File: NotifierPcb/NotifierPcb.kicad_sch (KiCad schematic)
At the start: 29 parts, among them IC1 CD4067BEE4, IC2 ESP32-WROOM-32E__8MB_, J1 RC_433_MHZ_RF, J2 UART_Conn, J3 Power_Conn, U1 HT75xx-1-SOT89

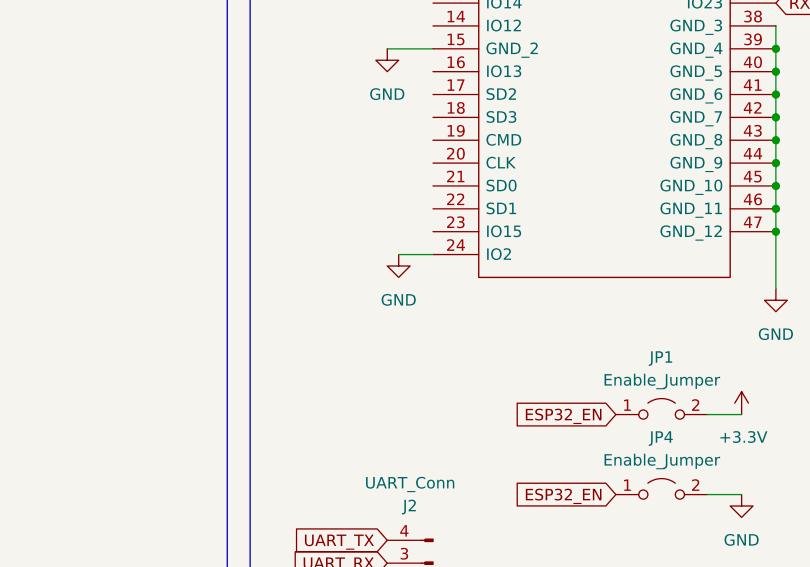
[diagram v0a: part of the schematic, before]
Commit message: reroute GND for headers
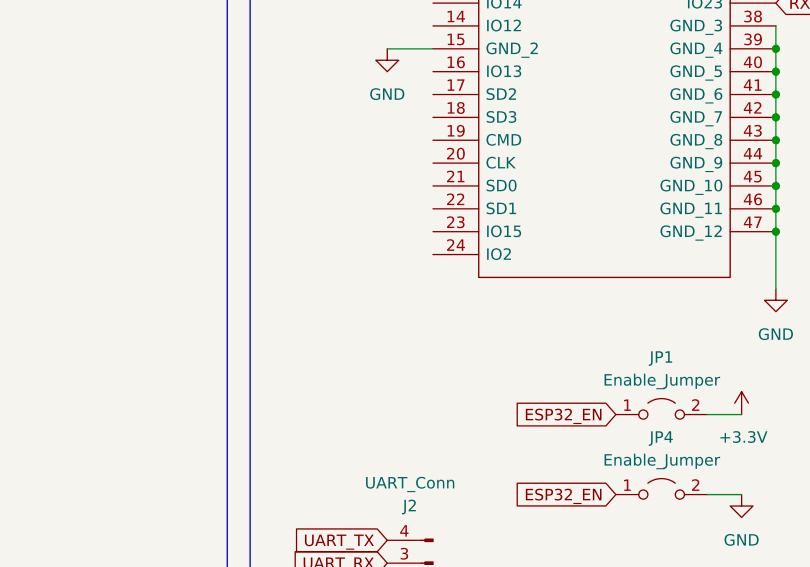
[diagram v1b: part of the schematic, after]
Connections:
- net GND: no longer IC2.24 (IO2)
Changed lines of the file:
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@@
-    (stroke (width 0) (type default) (color 0 0 0 0))
-  )
-  (wire (pts (xy 171.45 104.14) (xy 175.26 104.14))
     (stroke (width 0) (type default) (color 0 0 0 0))
   )
@@
     (pin "1")
     (pin "2")
-  )
-  (symbol (lib_id "power:GND") (at 171.45 104.14 0) (unit 1)
-    (in_bom yes) (on_board yes) (fields_autoplaced)
-    (property "Reference" "#PWR0105" (id 0) (at 171.45 110.49 0)
-      (effects (font (size 1.27 1.27)) hide)
-    )
-    (property "Value" "GND" (id 1) (at 171.45 109.22 0))
-    (property "Footprint" "" (id 2) (at 171.45 104.14 0)
-      (effects (font (size 1.27 1.27)) hide)
-    )
-    (property "Datasheet" "" (id 3) (at 171.45 104.14 0)
-      (effects (font (size 1.27 1.27)) hide)
-    )
-    (pin "1")
   )
   (symbol (lib_id "ESP32-WROOM-32E__8MB_:ESP32-WROOM-32E__8MB_") (at 175.26 45.72 0) (unit 1)
@@
       (reference "#PWR0104") (unit 1) (value "GND") (footprint "")
     )
-    (path "/5d99d38c-992c-4cfd-a466-550bac2fdf2c"
-      (reference "#PWR0105") (unit 1) (value "GND") (footprint "")
-    )
     (path "/12806a65-998f-4a2d-a376-f4dac4a43e49"

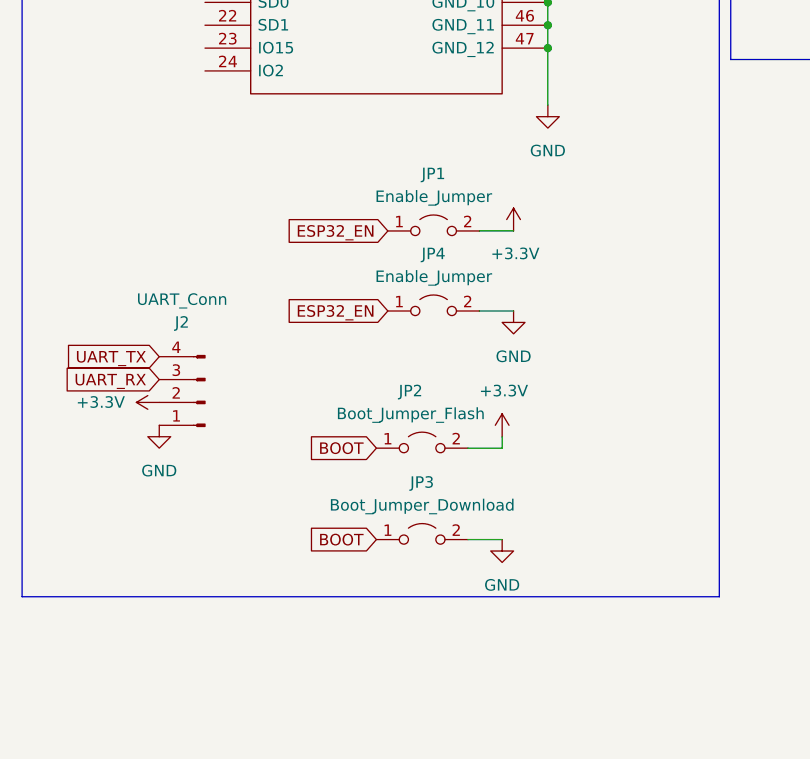
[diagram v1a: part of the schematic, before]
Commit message: remove unused flag selectors (default pin state)
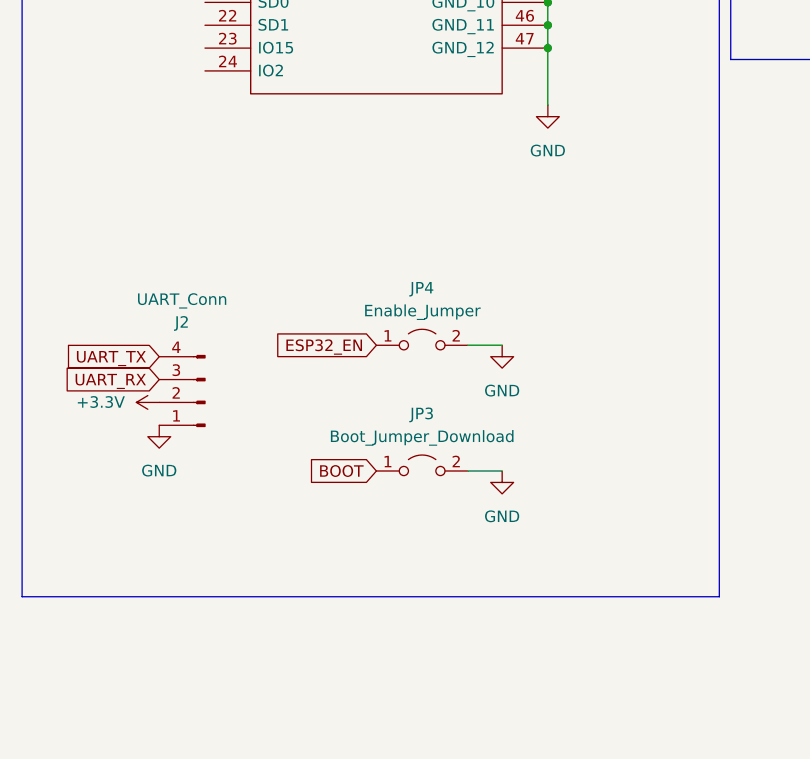
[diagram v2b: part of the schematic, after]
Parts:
- removed JP1: Enable_Jumper, Connector_PinHeader_2.54mm:PinHeader_1x02_P2.54mm_Vertical, symbol Jumper:Jumper_2_Open
- removed JP2: Boot_Jumper_Flash, Connector_PinHeader_2.54mm:PinHeader_1x02_P2.54mm_Vertical, symbol Jumper:Jumper_2_Open
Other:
- moved on the sheet: JP3, JP4

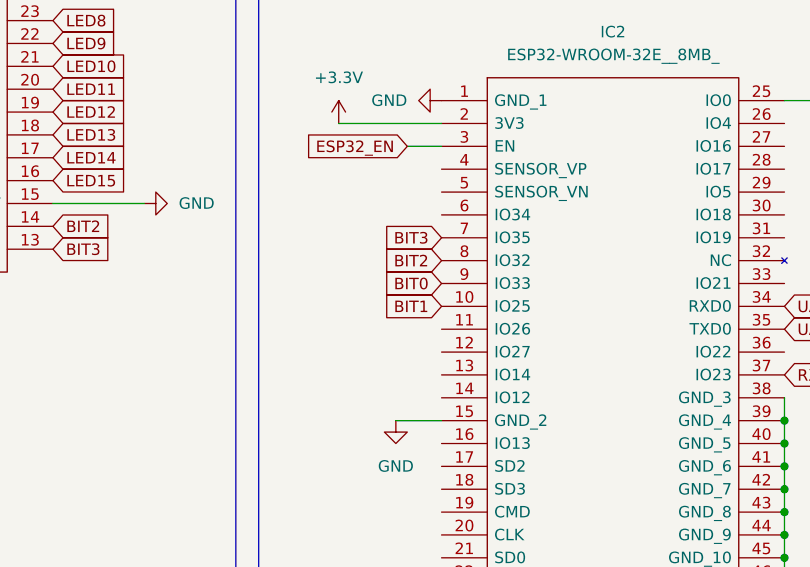
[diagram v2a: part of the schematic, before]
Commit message: FIX: using only-input pin
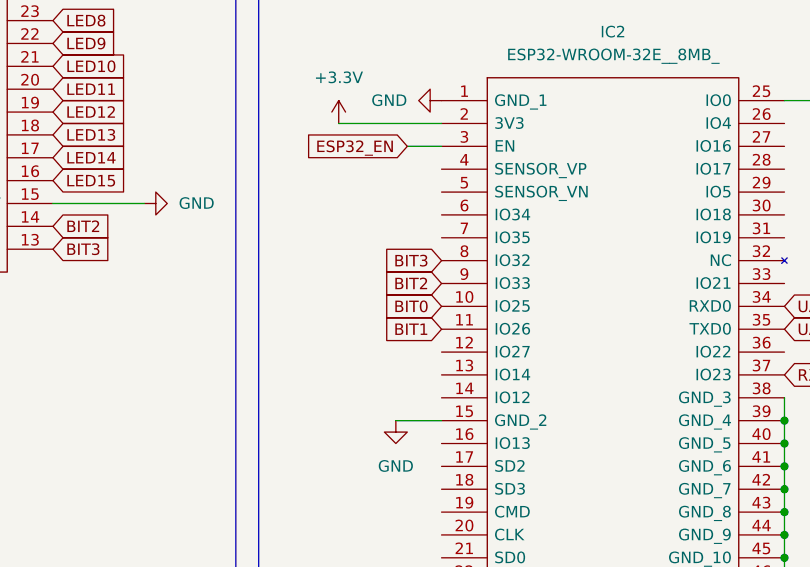
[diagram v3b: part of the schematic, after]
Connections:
- net BIT0: now also IC2.10 (IO25); no longer IC2.9 (IO33)
- net BIT1: now also IC2.11 (IO26); no longer IC2.10 (IO25)
- net BIT2: now also IC2.9 (IO33); no longer IC2.8 (IO32)
- net BIT3: now also IC2.8 (IO32); no longer IC2.7 (IO35)
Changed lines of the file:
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@@
     )
   )
-  (global_label "BIT2" (shape input) (at 175.26 63.5 180) (fields_autoplaced)
+  (global_label "BIT2" (shape input) (at 175.26 66.04 180) (fields_autoplaced)
     (effects (font (size 1.27 1.27)) (justify right))
-    (property "Intersheet References" "${INTERSHEET_REFS}" (id 0) (at 168.795 63.4206 0)
+    (property "Intersheet References" "${INTERSHEET_REFS}" (id 0) (at 168.795 65.9606 0)
       (effects (font (size 1.27 1.27)) (justify right) hide)
     )
@@
     )
   )
-  (global_label "BIT3" (shape input) (at 175.26 60.96 180) (fields_autoplaced)
+  (global_label "BIT3" (shape input) (at 175.26 63.5 180) (fields_autoplaced)
     (effects (font (size 1.27 1.27)) (justify right))
-    (property "Intersheet References" "${INTERSHEET_REFS}" (id 0) (at 168.795 60.8806 0)
+    (property "Intersheet References" "${INTERSHEET_REFS}" (id 0) (at 168.795 63.4206 0)
       (effects (font (size 1.27 1.27)) (justify right) hide)
     )
@@
     )
   )
-  (global_label "BIT1" (shape input) (at 175.26 68.58 180) (fields_autoplaced)
+  (global_label "BIT1" (shape input) (at 175.26 71.12 180) (fields_autoplaced)
     (effects (font (size 1.27 1.27)) (justify right))
-    (property "Intersheet References" "${INTERSHEET_REFS}" (id 0) (at 168.795 68.5006 0)
+    (property "Intersheet References" "${INTERSHEET_REFS}" (id 0) (at 168.795 71.0406 0)
       (effects (font (size 1.27 1.27)) (justify right) hide)
     )
@@
     )
   )
-  (global_label "BIT0" (shape input) (at 175.26 66.04 180) (fields_autoplaced)
+  (global_label "BIT0" (shape input) (at 175.26 68.58 180) (fields_autoplaced)
     (effects (font (size 1.27 1.27)) (justify right))
-    (property "Intersheet References" "${INTERSHEET_REFS}" (id 0) (at 168.795 65.9606 0)
+    (property "Intersheet References" "${INTERSHEET_REFS}" (id 0) (at 168.795 68.5006 0)
       (effects (font (size 1.27 1.27)) (justify right) hide)
     )

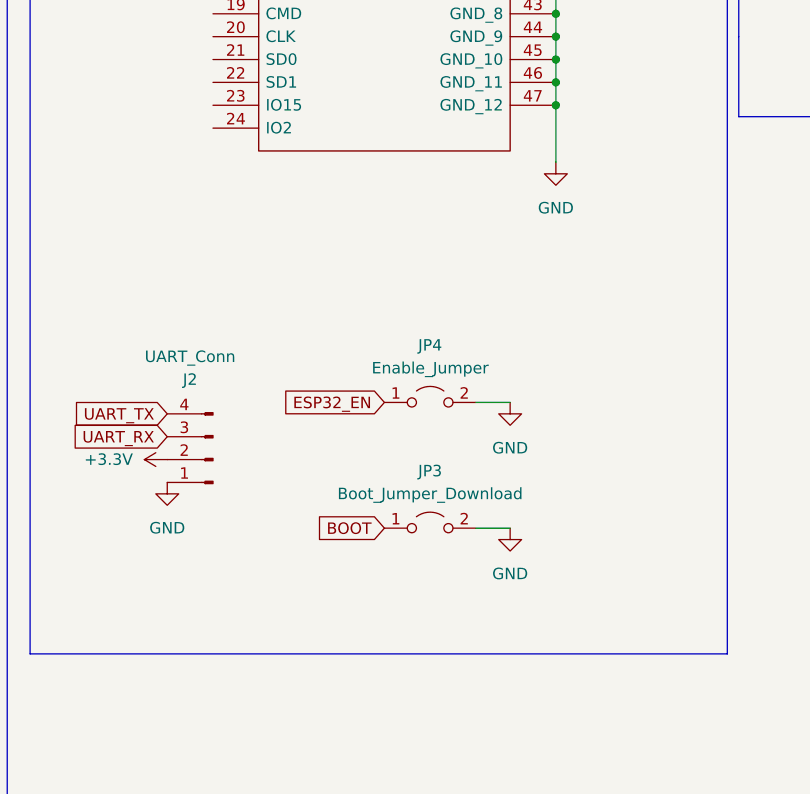
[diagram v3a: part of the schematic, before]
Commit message: add pullup resistor for strapping pins
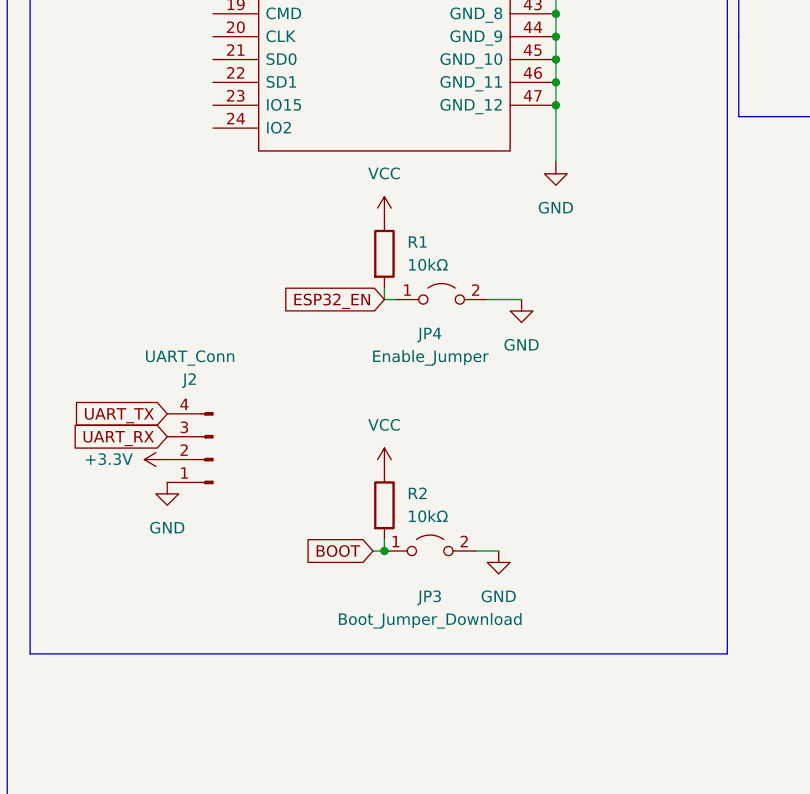
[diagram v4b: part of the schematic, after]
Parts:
- added R1, R2: 10kΩ, Resistor_THT:R_Axial_DIN0204_L3.6mm_D1.6mm_P2.54mm_Vertical, symbol Device:R
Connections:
- net BOOT: now also R2.2
- net ESP32_EN: now also R1.2
- new net VCC: R1.1, R2.1
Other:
- moved on the sheet: JP3, JP4

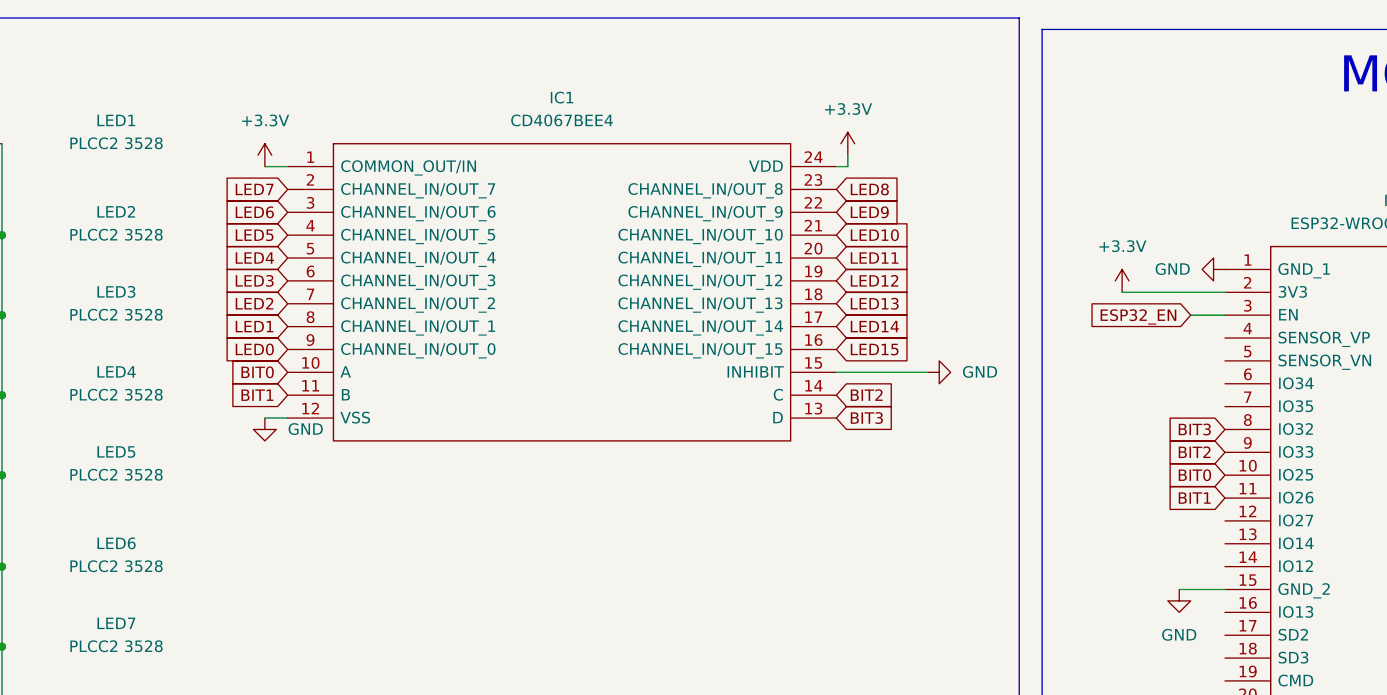
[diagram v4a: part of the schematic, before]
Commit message: control demux input
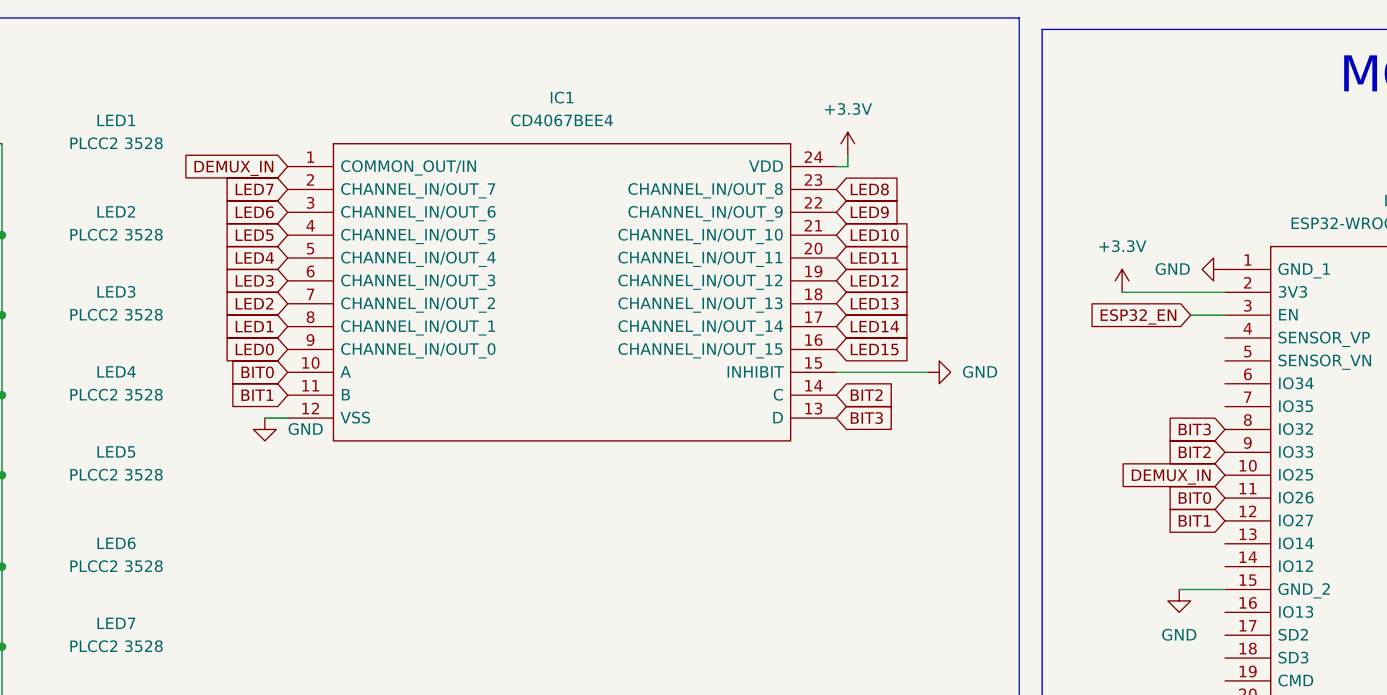
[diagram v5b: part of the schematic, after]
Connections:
- net +3.3V: no longer IC1.1 (COMMON_OUT/IN)
- net BIT0: now also IC2.11 (IO26); no longer IC2.10 (IO25)
- net BIT1: now also IC2.12 (IO27); no longer IC2.11 (IO26)
- new net DEMUX_IN: IC1.1 (COMMON_OUT/IN), IC2.10 (IO25)
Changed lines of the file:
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@@
-    (stroke (width 0) (type default) (color 0 0 0 0))
-  )
-  (wire (pts (xy 68.58 34.29) (xy 71.12 34.29))
     (stroke (width 0) (type default) (color 0 0 0 0))
   )
@@
     )
   )
-  (global_label "BIT1" (shape input) (at 175.26 71.12 180) (fields_autoplaced)
-    (effects (font (size 1.27 1.27)) (justify right))
-    (property "Intersheet References" "${INTERSHEET_REFS}" (id 0) (at 168.795 71.0406 0)
+  (global_label "BIT1" (shape input) (at 175.26 73.66 180) (fields_autoplaced)
+    (effects (font (size 1.27 1.27)) (justify right))
+    (property "Intersheet References" "${INTERSHEET_REFS}" (id 0) (at 168.795 73.5806 0)
       (effects (font (size 1.27 1.27)) (justify right) hide)
     )
@@
     )
   )
-  (global_label "BIT0" (shape input) (at 175.26 68.58 180) (fields_autoplaced)
-    (effects (font (size 1.27 1.27)) (justify right))
-    (property "Intersheet References" "${INTERSHEET_REFS}" (id 0) (at 168.795 68.5006 0)
+  (global_label "BIT0" (shape input) (at 175.26 71.12 180) (fields_autoplaced)
+    (effects (font (size 1.27 1.27)) (justify right))
+    (property "Intersheet References" "${INTERSHEET_REFS}" (id 0) (at 168.795 71.0406 0)
       (effects (font (size 1.27 1.27)) (justify right) hide)
     )
@@
     )
   )
+  (global_label "DEMUX_IN" (shape input) (at 71.12 34.29 180) (fields_autoplaced)
+    (effects (font (size 1.27 1.27)) (justify right))
+    (property "Intersheet References" "${INTERSHEET_REFS}" (id 0) (at 59.3936 34.2106 0)
+      (effects (font (size 1.27 1.27)) (justify right) hide)
+    )
+  )
   (global_label "BOOT" (shape input) (at 217.17 45.72 0) (fields_autoplaced)
     (effects (font (size 1.27 1.27)) (justify left))
     (property "Intersheet References" "${INTERSHEET_REFS}" (id 0) (at 224.4817 45.6406 0)
       (effects (font (size 1.27 1.27)) (justify left) hide)
+    )
+  )
+  (global_label "DEMUX_IN" (shape input) (at 175.26 68.58 180) (fields_autoplaced)
+    (effects (font (size 1.27 1.27)) (justify right))
+    (property "Intersheet References" "${INTERSHEET_REFS}" (id 0) (at 163.5336 68.5006 0)
+      (effects (font (size 1.27 1.27)) (justify right) hide)
     )
   )
@@
     (pin "1")
     (pin "2")
-  )
-  (symbol (lib_id "power:+3.3V") (at 68.58 34.29 0) (unit 1)
-    (in_bom yes) (on_board yes) (fields_autoplaced)
-    (property "Reference" "#PWR02" (id 0) (at 68.58 38.1 0)
-      (effects (font (size 1.27 1.27)) hide)
-    )
-    (property "Value" "+3.3V" (id 1) (at 68.58 29.21 0))
-    (property "Footprint" "" (id 2) (at 68.58 34.29 0)
-      (effects (font (size 1.27 1.27)) hide)
-    )
-    (property "Datasheet" "" (id 3) (at 68.58 34.29 0)
-      (effects (font (size 1.27 1.27)) hide)
-    )
-    (pin "1")
   )
   (symbol (lib_id "RC_433_RX:RC_433_MHZ_RF") (at 256.54 41.91 0) (unit 1)
@@
       (reference "#PWR01") (unit 1) (value "+3.3V") (footprint "")
     )
-    (path "/2772f406-ea45-4374-afd7-1ed6e3e8084e"
-      (reference "#PWR02") (unit 1) (value "+3.3V") (footprint "")
-    )
     (path "/ba17a5d4-03e3-4f0c-8953-4fd95bbdcc72"
